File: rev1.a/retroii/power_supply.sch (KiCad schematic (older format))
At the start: 40 parts, among them J10 BARREL_JACK, J11 Conn_02x10, SW2 SPST2, U11 LM2576-12, U12 LM2576-5, U13 LM2576-12, U14 LM2576-3.3, U15 LM2576-5

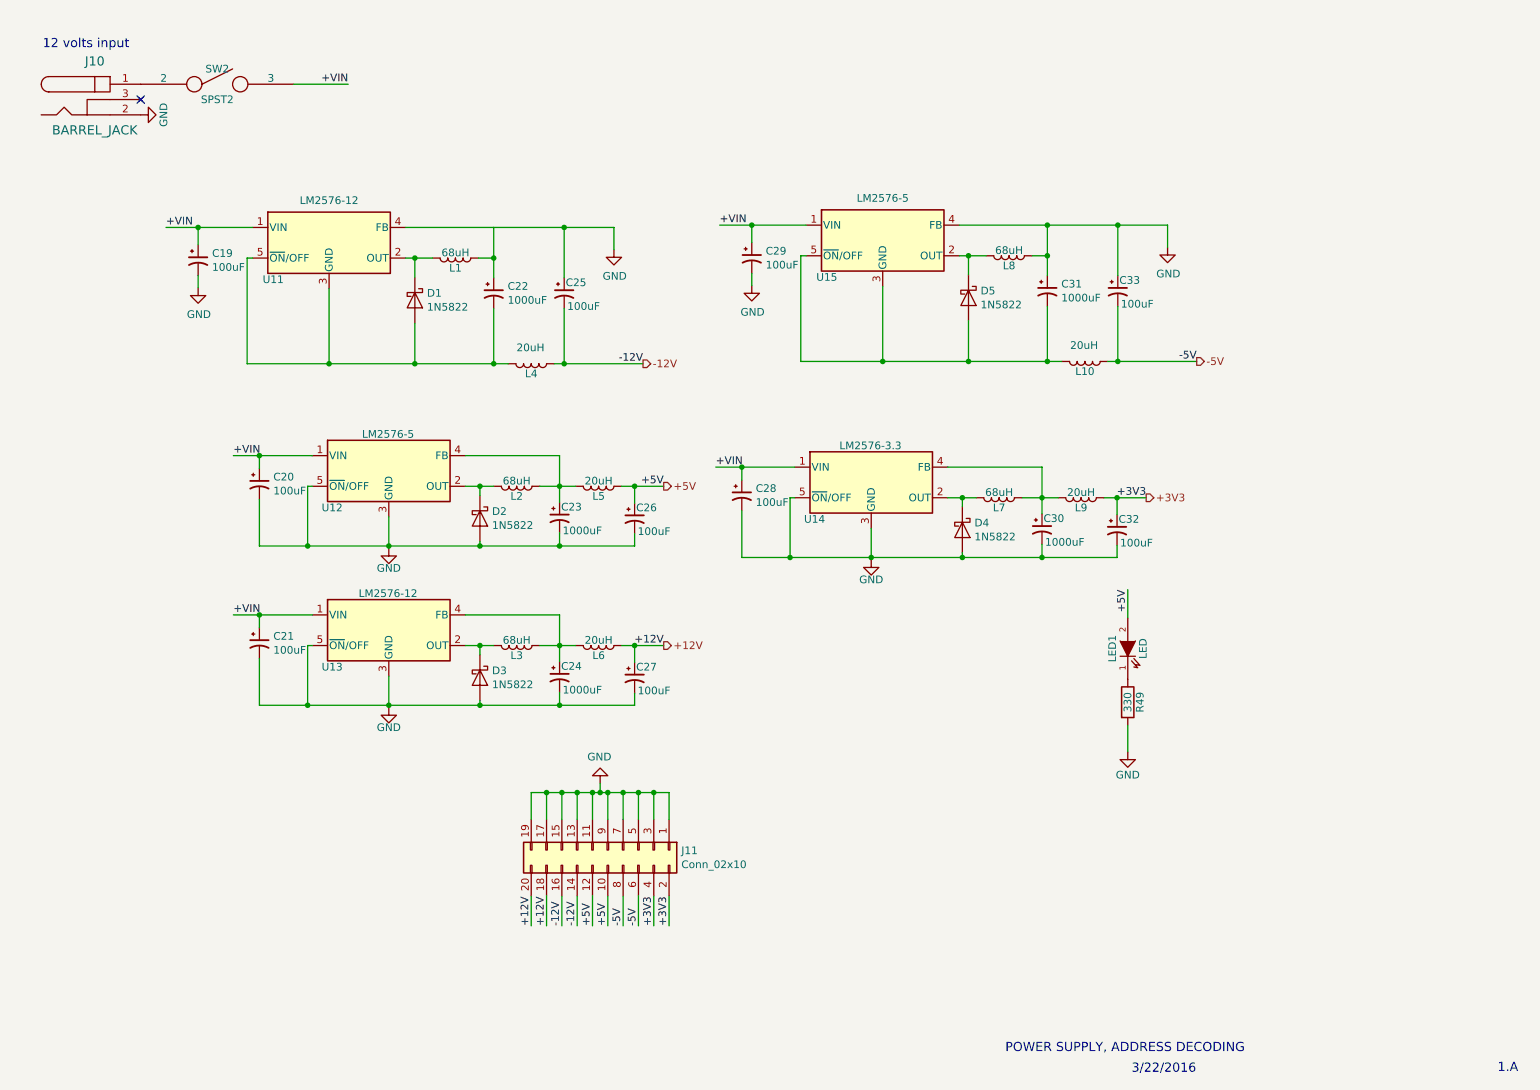
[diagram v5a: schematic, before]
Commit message: added support for lm2576 adjustable version
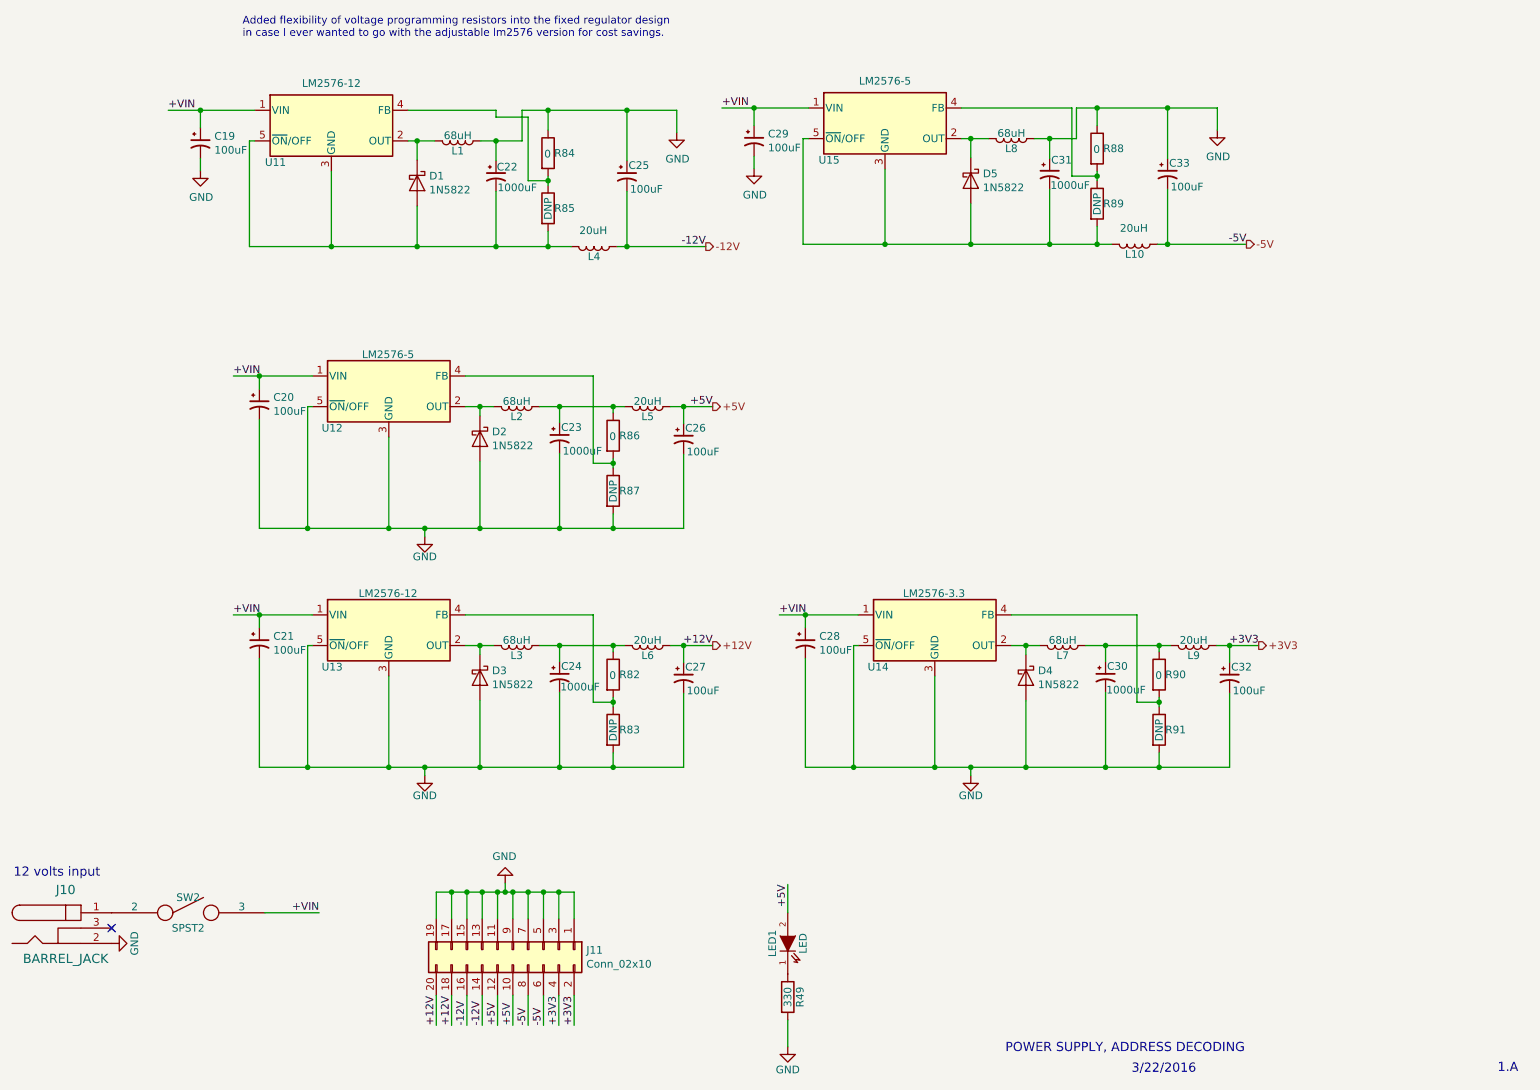
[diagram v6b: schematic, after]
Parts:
- added R82, R84, R86, R88, R90: 0, retroii_footprints:R_Axial_DIN0207_L6.3mm_D2.5mm_P10.16mm_Horizontal, symbol 6502:R
- added R83, R85, R87, R89, R91: DNP, retroii_footprints:R_Axial_DIN0207_L6.3mm_D2.5mm_P10.16mm_Horizontal, symbol 6502:R
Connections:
- net GND: now also R83.2, R84.1, R87.2, R88.1, R91.2; no longer U11.4 (FB), U15.4 (FB)
- net at C22.2, D1.2 (A), L4.2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: now also R85.2
- net at C23.1, L2.1, L5.2: now also R86.1; no longer U12.4 (FB)
- net at C24.1, L3.1, L6.2: now also R82.1; no longer U13.4 (FB)
- net at C31.2, D5.2 (A), L10.2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: now also R89.2
- net at C30.1, L7.1, L9.2: now also R90.1; no longer U14.4 (FB)
- new net: R86.2, R87.1, U12.4 (FB)
- new net: R84.2, R85.1, U11.4 (FB)
- new net: R82.2, R83.1, U13.4 (FB)
- new net: R88.2, R89.1, U15.4 (FB)
- new net: R90.2, R91.1, U14.4 (FB)
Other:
- note added: "Added flexibility of voltage programming resistors into the fixed regulator design\nin case I ever wanted to go with the adjustable lm2576 version for cost savings."
- moved on the sheet: C19, C20, C22, C23, C25, C26, C27, C28, C29, C30, C31, C32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

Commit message: added more in/out caps for psu. finished initial layout of psu.
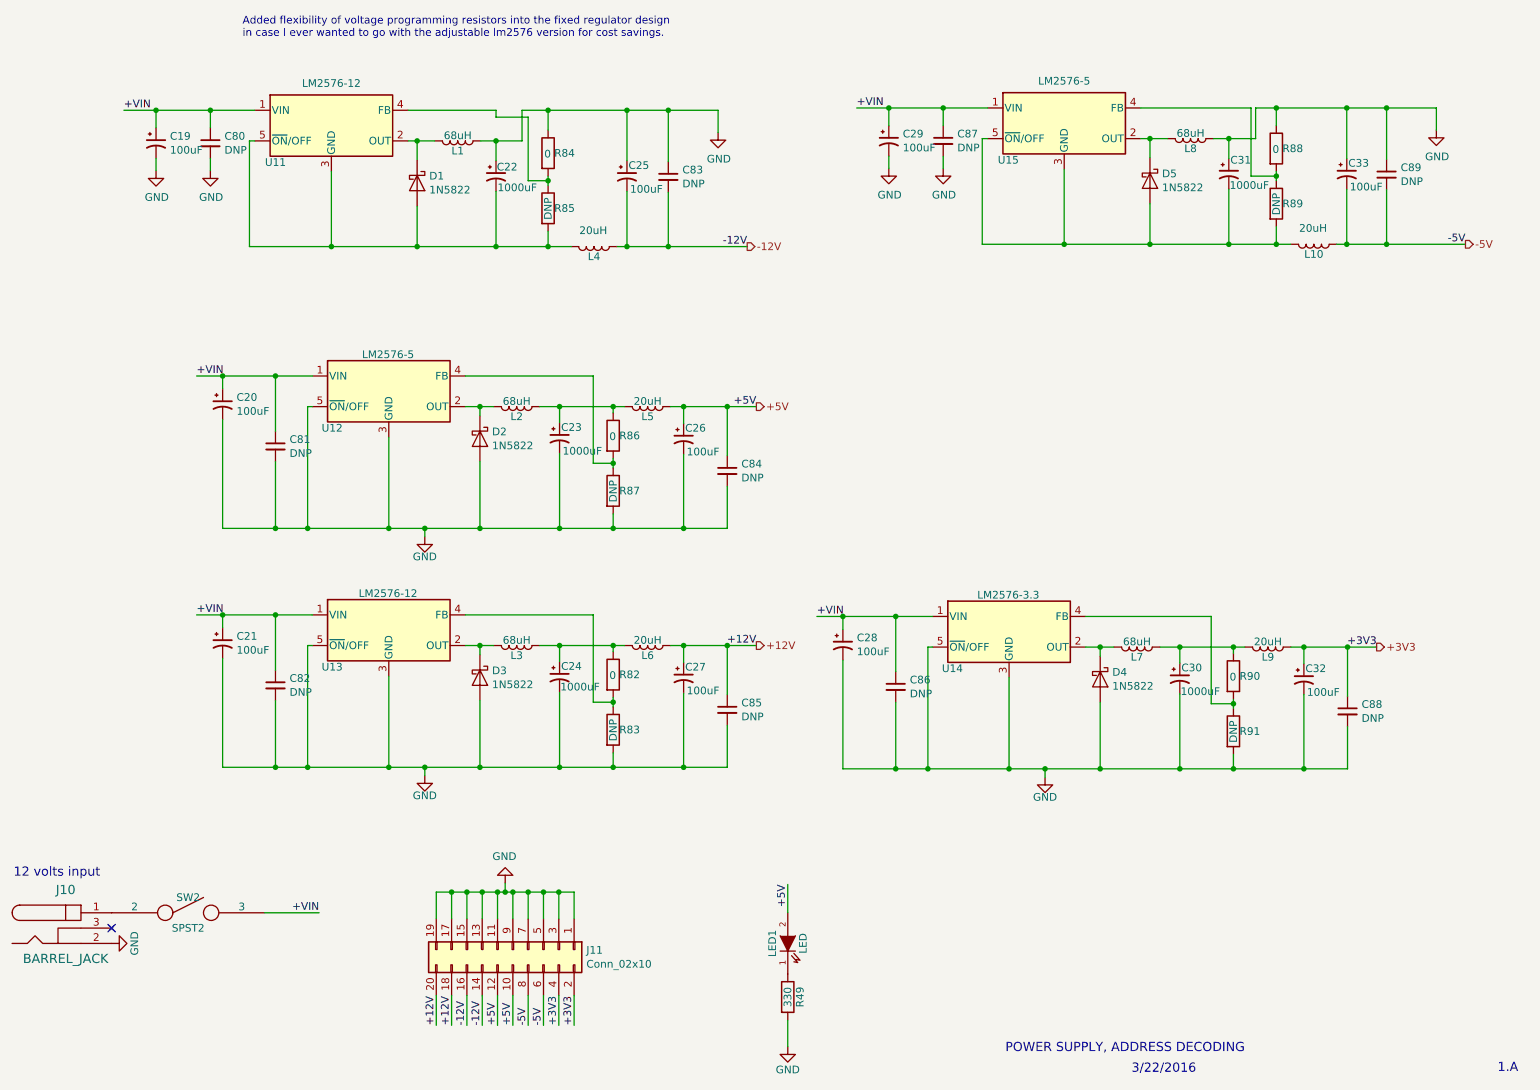
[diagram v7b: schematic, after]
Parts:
- added C80, C81, C82, C83, C84, C85, C86, C87, C88, C89: DNP, retroii_footprints:C_Disc_D3.0mm_W2.0mm_P2.50mm, symbol Device:C_Small
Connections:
- net +12V: now also C85.1
- net +3V3: now also C88.1
- net +5V: now also C84.1
- net +VIN: now also C80.1, C81.1, C82.1, C86.1, C87.1
- net -12V: now also C83.2
- net -5V: now also C89.2
- net GND: now also C80.2, C81.2, C82.2, C83.1, C84.2, C85.2, C86.2, C87.2, C88.2, C89.1
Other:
- moved on the sheet: C19, C20, C21, C28, C29, C30, C31, C32, C33, D4, D5, L10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

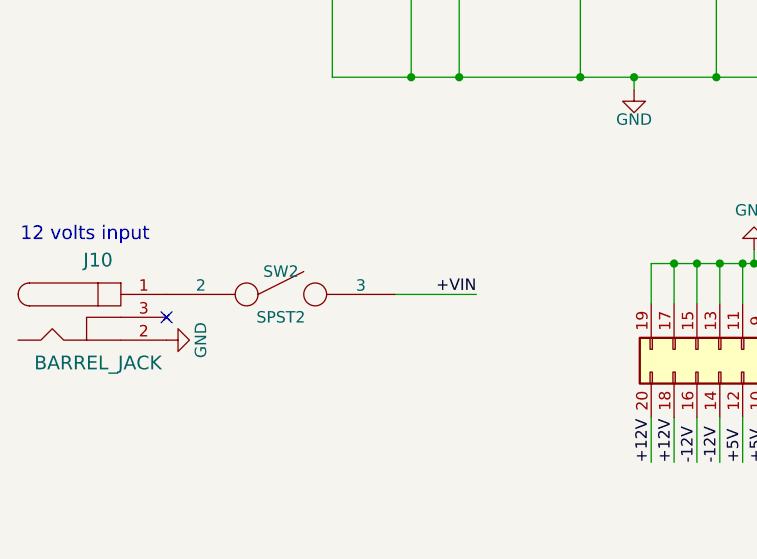
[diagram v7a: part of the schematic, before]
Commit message: added a fuse
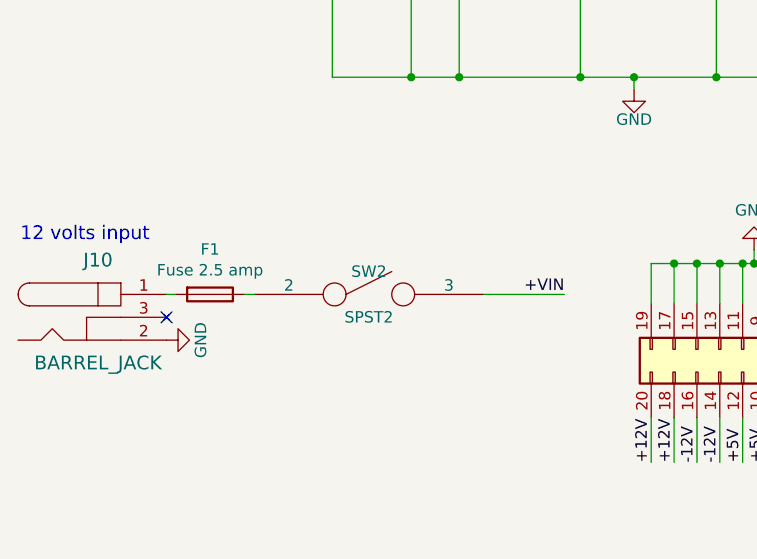
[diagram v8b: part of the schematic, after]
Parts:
- added F1: Fuse 2.5 amp, retroii_footprints:littlefuse_5.08_radial, symbol Device:Fuse
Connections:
- net at J10.1: now also F1.2; no longer SW2.2
- new net: F1.1, SW2.2
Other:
- moved on the sheet: SW2
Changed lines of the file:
@@
 L 6502:SPST2 SW2
 U 1 1 5C8ADA13
-P 2025 6590
+P 2410 6590
 AR Path="/5C8AA2BF/5C8ADA13" Ref="SW2"  Part="1"
 AR Path="/5C8AABED/5C8ADA13" Ref="SW?"  Part="1"
-F 0 "SW2" H 2025 6690 50  0000 C CNN
-F 1 "SPST2" H 2025 6490 50  0000 C CNN
-F 2 "retroii_footprints:SW_Micro_Right_Angle_SPST" H 2025 6590 50  0001 C CNN
-F 3 "" H 2025 6590 50  0000 C CNN
-	1    2025 6590
+F 0 "SW2" H 2410 6690 50  0000 C CNN
+F 1 "SPST2" H 2410 6490 50  0000 C CNN
+F 2 "retroii_footprints:SW_Micro_Right_Angle_SPST" H 2410 6590 50  0001 C CNN
+F 3 "" H 2410 6590 50  0000 C CNN
+	1    2410 6590
 	1    0    0    -1
 $EndComp
@@
 	5260 3285 5260 3395
 Wire Wire Line
-	2525 6590 2880 6590
-Text Label 2880 6590 2    50   ~ 0
+	2910 6590 3265 6590
+Text Label 3265 6590 2    50   ~ 0
 +VIN
 $Comp
@@
 Connection ~ 9850 1335
 Connection ~ 9850 2225
+$Comp
+L Device:Fuse F1
+U 1 1 5D375059
+P 1715 6590
+F 0 "F1" V 1518 6590 50  0000 C CNN
+F 1 "Fuse 2.5 amp" V 1609 6590 50  0000 C CNN
+F 2 "retroii_footprints:littlefuse_5.08_radial" V 1645 6590 50  0001 C CNN
+F 3 "~" H 1715 6590 50  0001 C CNN
+	1    1715 6590
+	0    1    1    0
+$EndComp
+Wire Wire Line
+	1525 6590 1565 6590
+Wire Wire Line
+	1865 6590 1910 6590
 $EndSCHEMATC
